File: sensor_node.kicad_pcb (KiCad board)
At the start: 2 copper layers, 92 parts, among them J1 Conn_01x06_Male, J2 Conn_01x03, J3 USB_B_Micro, J4 Conn_01x02_Female, J5 Conn_01x06_Male, J6 Conn_01x04_Male, J7 Conn_01x08_Male, Q1 Q_NMOS_DGS, Q2 Q_NMOS_DGS, Q3 Q_PMOS_DGS, Q4 Q_PMOS_DGS, SW1 SW_Push, SW2 SW_Push, U1 STM32L053R6Tx, U2 ESP-12F, U3 BME680, U4 Si1133, U5 USBLC6-2SC6, U6 BQ27441-G1, U7 BQ24075, U8 TPS826711, U9 LMZ21700, Y1 32.764kHz

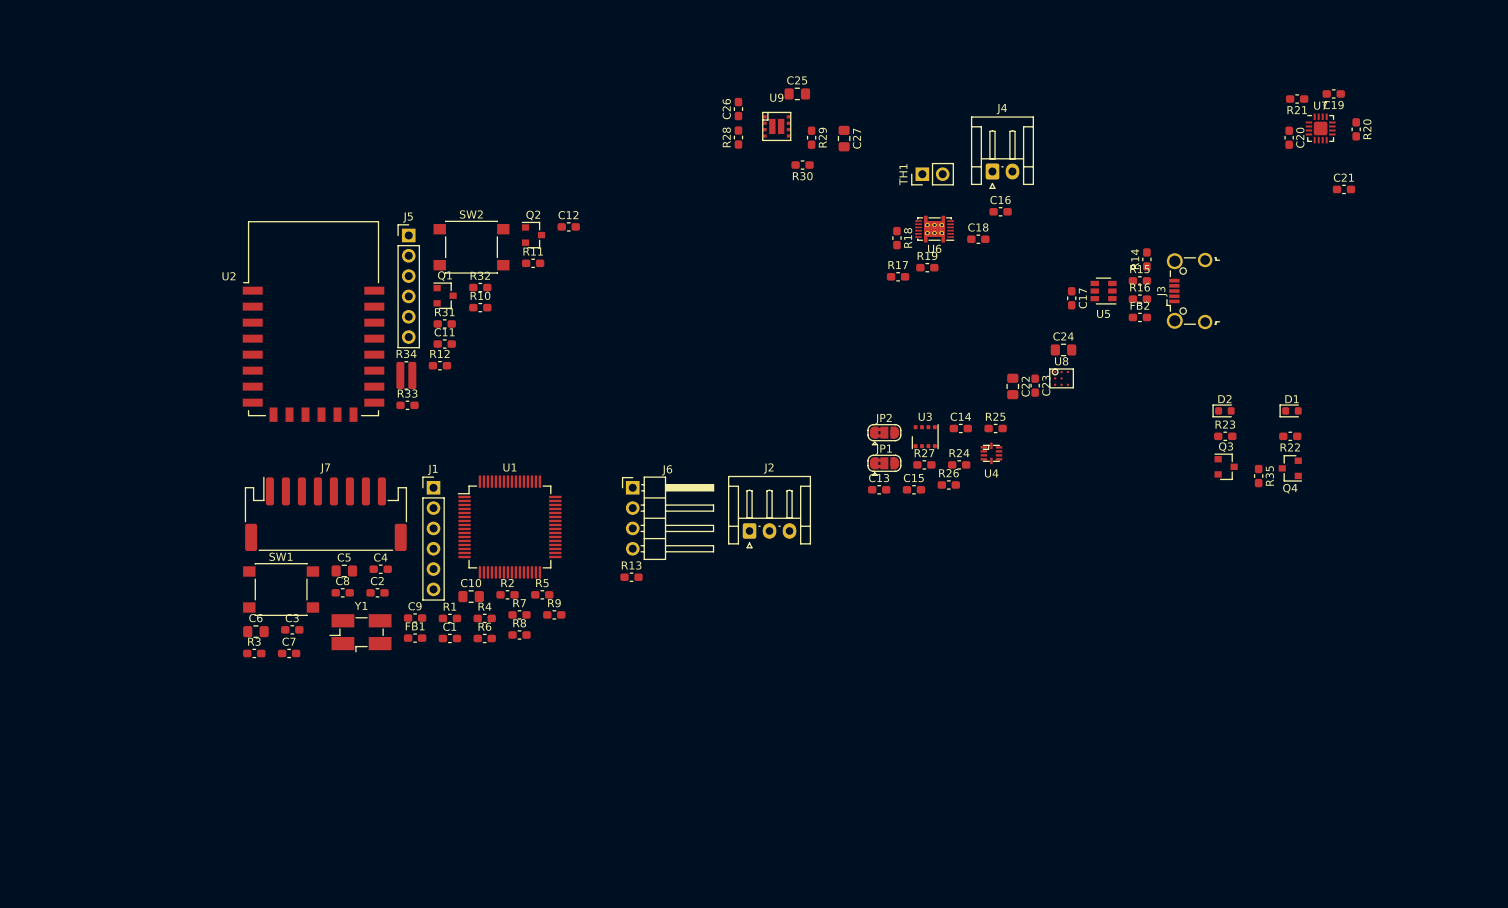
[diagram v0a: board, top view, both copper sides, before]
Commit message: work on layout and smaller changes to schematic
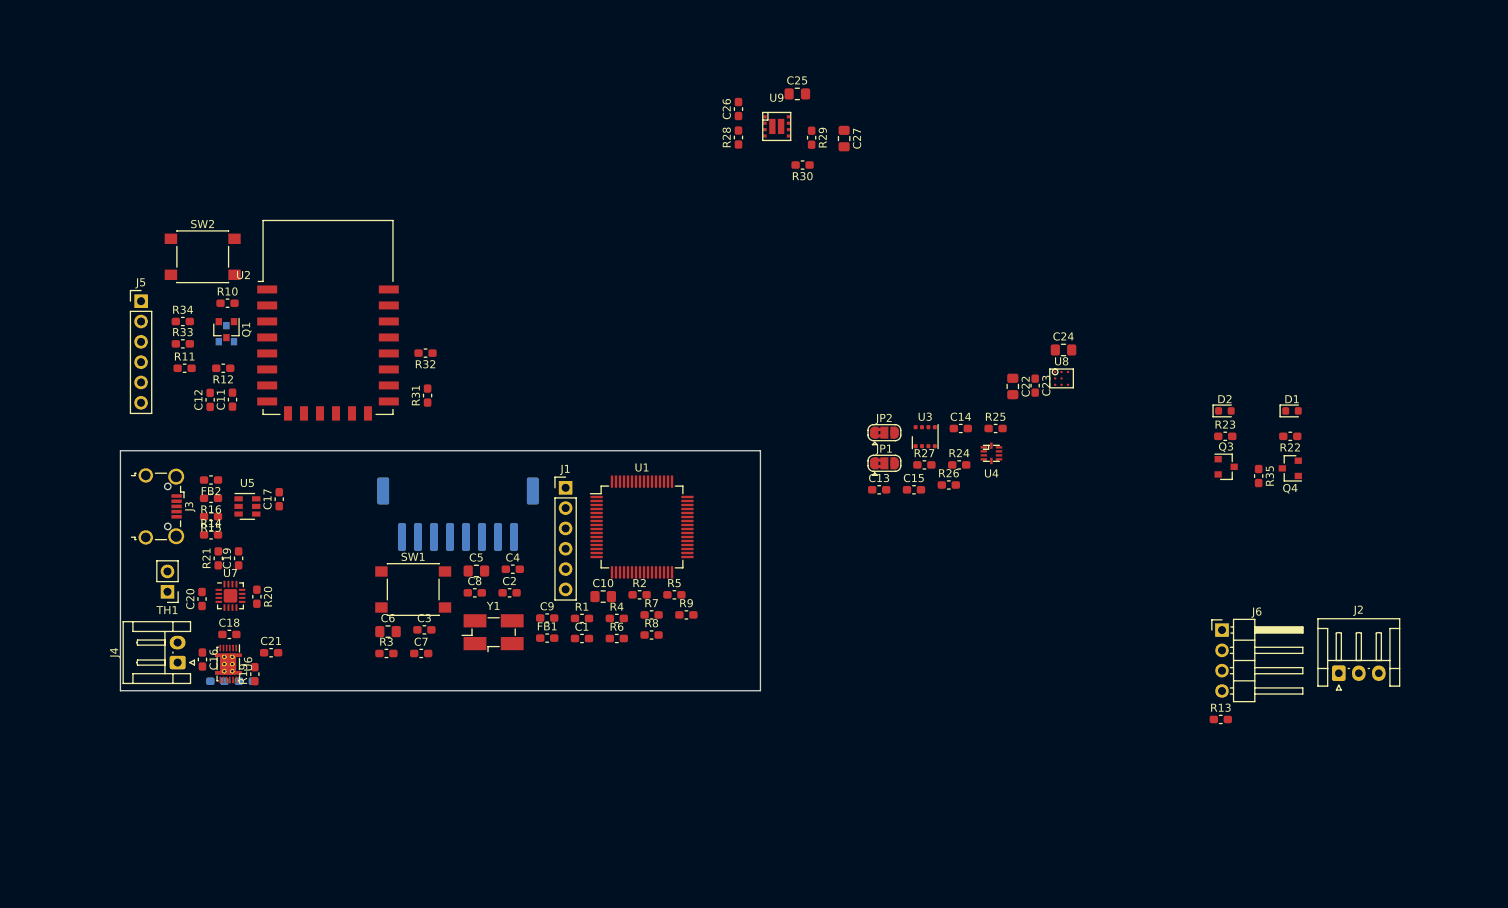
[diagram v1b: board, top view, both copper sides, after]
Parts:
- J7, Q2, R17, R18: moved to B.Cu
- R34: footprint Resistor_SMD:R_0612_1632Metric -> Resistor_SMD:R_0603_1608Metric_Pad1.05x0.95mm_HandSolder
- moved R20 149.3 mm to (67.1, 88.3)
- moved C19 148.7 mm to (64.8, 83.5), turned to 90 degrees
- moved U7 148.3 mm to (63.8, 88.1)
- moved C20 147.6 mm to (60.2, 88.5), turned to 90 degrees
- moved R21 146.6 mm to (62.2, 83.5), turned to 90 degrees
- moved C21 146.1 mm to (68.8, 95.2)
- moved J3 131.3 mm to (55.1, 77.0), turned to 270 degrees
- moved R14 121.9 mm to (61.3, 80.5), turned to 0 degrees
- moved R15 119.8 mm to (61.3, 78.2), turned to 180 degrees
- moved J4 118.9 mm to (57.1, 96.5), turned to 90 degrees
- moved R16 118.7 mm to (61.3, 75.9), turned to 180 degrees
- moved FB2 117.9 mm to (61.3, 73.7), turned to 180 degrees
- moved C16 114.4 mm to (60.2, 96.1), turned to 270 degrees
- moved U5 110.4 mm to (65.9, 77.0), turned to 0 degrees
- moved TH1 107.8 mm to (55.9, 87.6), turned to 180 degrees
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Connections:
- J4 pad 1: Net-(J4-Pad1) -> /power_supply/VBAT_P
- J4 pad 2: Net-(J4-Pad2) -> GND
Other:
- board outline added: 80 x 30 mm

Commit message: change mcu to smaller one
change connectors
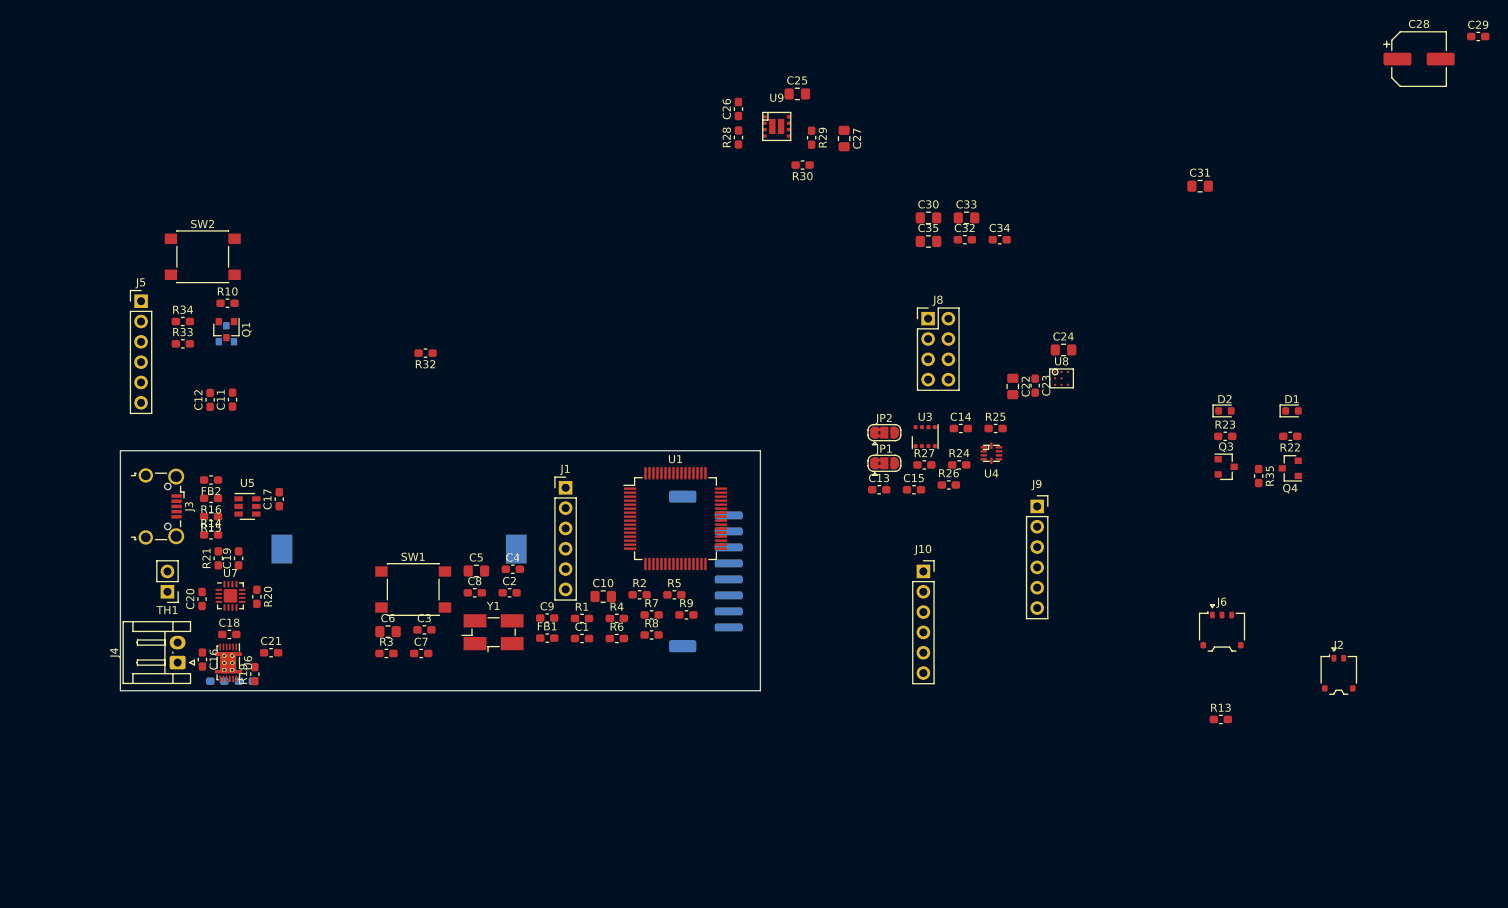
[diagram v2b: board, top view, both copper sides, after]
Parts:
- removed R11, R12, R31: 10k, Resistor_SMD:R_0603_1608Metric_Pad1.05x0.95mm_HandSolder
- removed U2: ESP-12F, RF_Module:ESP-12E
- added BT1: Battery_Cell, Battery:BatteryHolder_Keystone_1060_1x2032, B.Cu at (84.8, 82.3)
- added C28: 10uF, Capacitor_SMD:CP_Elec_6.3x3, F.Cu at (212.3, 21.0)
- added C29: 100nF, Capacitor_SMD:C_0603_1608Metric_Pad1.05x0.95mm_HandSolder, F.Cu at (219.7, 18.2)
- added C30: 10uF, Capacitor_SMD:C_0805_2012Metric_Pad1.15x1.40mm_HandSolder, F.Cu at (151.0, 40.9)
- added C31: 10uF, Capacitor_SMD:C_0805_2012Metric_Pad1.15x1.40mm_HandSolder, F.Cu at (185.0, 36.9)
- added C32: 100nF, Capacitor_SMD:C_0603_1608Metric_Pad1.05x0.95mm_HandSolder, F.Cu at (155.6, 43.6)
- added C33: 10uF, Capacitor_SMD:C_0805_2012Metric_Pad1.15x1.40mm_HandSolder, F.Cu at (155.8, 40.9)
- added C34: 100nF, Capacitor_SMD:C_0603_1608Metric_Pad1.05x0.95mm_HandSolder, F.Cu at (159.9, 43.6)
- added C35: 10uF, Capacitor_SMD:C_0805_2012Metric_Pad1.15x1.40mm_HandSolder, F.Cu at (151.0, 43.8)
- added J10: Conn_01x06, Connector_PinSocket_2.54mm:PinSocket_1x06_P2.54mm_Vertical, F.Cu at (150.4, 85.1)
- added J8: Conn_02x04_Odd_Even, Connector_PinHeader_2.54mm:PinHeader_2x04_P2.54mm_Vertical, F.Cu at (151.0, 53.5)
- added J9: Conn_01x06_Male, Connector_PinSocket_2.54mm:PinSocket_1x06_P2.54mm_Vertical, F.Cu at (164.6, 77.0)
- J2: footprint Connector_JST:JST_EH_S3B-EH_1x03_P2.50mm_Horizontal -> Connector_Molex:Molex_Pico-EZmate_78171-0002_1x02-1MP_P1.20mm_Vertical
- J6: footprint Connector_PinHeader_2.54mm:PinHeader_1x04_P2.54mm_Horizontal -> Connector_Molex:Molex_Pico-EZmate_78171-0003_1x03-1MP_P1.20mm_Vertical
- U1: value STM32L053R6Tx -> STM32L063R8Tx
- moved J7 31.8 mm to (123.2, 85.1), turned to 90 degrees
- moved U1 4.31 mm to (119.4, 78.5)
- moved U6 0.14 mm to (63.5, 96.5)
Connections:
- net /mcu.sch/PC0 renamed Net-(U1-Pad8)
- net /mcu.sch/PC1 renamed Net-(U1-Pad9)
- net /mcu.sch/PC10 renamed Net-(U1-Pad51)
- net /mcu.sch/PC11 renamed Net-(U1-Pad52)
- net /mcu.sch/PC12 renamed Net-(U1-Pad53)
- net /mcu.sch/PC13 renamed Net-(U1-Pad2)
- net /mcu.sch/PC14 renamed Net-(U1-Pad3)
- net /mcu.sch/PC15 renamed Net-(U1-Pad4)
- net /mcu.sch/PC2 renamed Net-(U1-Pad10)
- net /mcu.sch/PC3 renamed Net-(U1-Pad11)
- net /mcu.sch/PC4 renamed Net-(U1-Pad24)
- net /mcu.sch/PC5 renamed Net-(U1-Pad25)
- net /mcu.sch/PC6 renamed Net-(U1-Pad37)
- net /mcu.sch/PC7 renamed Net-(U1-Pad38)
- net /mcu.sch/PC8 renamed Net-(U1-Pad39)
- net /mcu.sch/PC9 renamed Net-(U1-Pad40)
- J5 pad 1: /ESP_RX -> /wireless/ESP_TX
- J5 pad 4: /ESP_TX -> /wireless/ESP_RX
- R5 pad 1: /mcu.sch/I2C1_SCL -> /SCL
- R6 pad 1: /mcu.sch/I2C1_SDA -> /SDA
- U1 pad 5: Net-(C8-Pad1) -> Net-(U1-Pad5)
- U1 pad 6: Net-(R1-Pad1) -> Net-(U1-Pad6)
- U1 pad 60: Net-(R2-Pad2) -> Net-(U1-Pad60)
- U1 pad 61: /mcu.sch/I2C1_SCL -> /SCL
- U1 pad 62: /mcu.sch/I2C1_SDA -> /SDA

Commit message: strip of some components and use more external modules
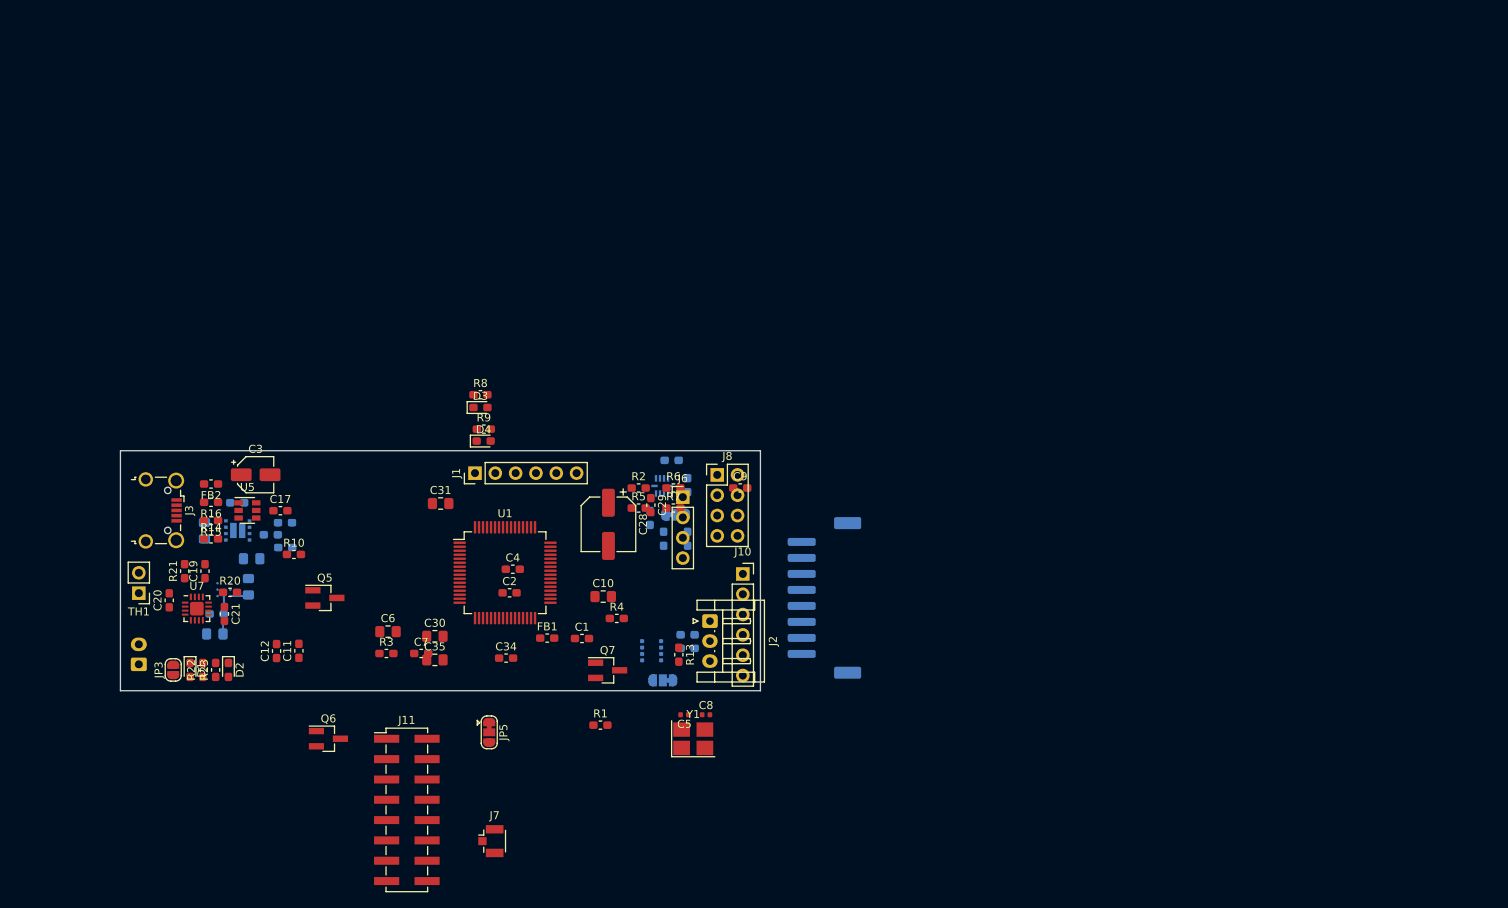
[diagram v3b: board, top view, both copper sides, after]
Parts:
- removed BT1: Battery_Cell, Battery:BatteryHolder_Keystone_1060_1x2032
- removed C16: 1uF, Capacitor_SMD:C_0603_1608Metric_Pad1.05x0.95mm_HandSolder
- removed C18: 0.47uF, Capacitor_SMD:C_0603_1608Metric_Pad1.05x0.95mm_HandSolder
- removed C32: 100nF, Capacitor_SMD:C_0603_1608Metric_Pad1.05x0.95mm_HandSolder
- removed C33: 10uF, Capacitor_SMD:C_0805_2012Metric_Pad1.15x1.40mm_HandSolder
- removed J9: Conn_01x06_Male, Connector_PinSocket_2.54mm:PinSocket_1x06_P2.54mm_Vertical
- removed Q1, Q2: Q_NMOS_DGS, Package_TO_SOT_SMD:SOT-23
- removed Q3, Q4: Q_PMOS_DGS, Package_TO_SOT_SMD:SOT-23
- removed R17: 10m, Resistor_SMD:R_0603_1608Metric_Pad1.05x0.95mm_HandSolder
- removed R18, R19, R32: 10k, Resistor_SMD:R_0603_1608Metric_Pad1.05x0.95mm_HandSolder
- removed R33, R34: R, Resistor_SMD:R_0603_1608Metric_Pad1.05x0.95mm_HandSolder
- removed R35: 20k, Resistor_SMD:R_0603_1608Metric_Pad1.05x0.95mm_HandSolder
- removed SW1, SW2: SW_Push, Button_Switch_SMD:SW_Push_1P1T_NO_6x6mm_H9.5mm
- removed U6: BQ27441-G1, Package_SON:Texas_S-PDSO-N12
- added D3: LED, LED_SMD:LED_0603_1608Metric_Pad1.05x0.95mm_HandSolder, F.Cu at (95.0, 64.6)
- added D4: LED, LED_SMD:LED_0603_1608Metric_Pad1.05x0.95mm_HandSolder, F.Cu at (95.4, 68.8)
- added J11: Conn_02x08_Counter_Clockwise, Connector_PinHeader_2.54mm:PinHeader_2x08_P2.54mm_Vertical_SMD, F.Cu at (85.8, 114.9)
- added JP3: Jumper_2_Open, Jumper:SolderJumper-2_P1.3mm_Open_RoundedPad1.0x1.5mm, F.Cu at (56.6, 97.4)
- added JP5: SolderJumper_3_Bridged12, Jumper:SolderJumper-3_P1.3mm_Bridged12_RoundedPad1.0x1.5mm, F.Cu at (96.1, 105.2)
- added Q5: Q_PMOS_GSD, Package_TO_SOT_SMD:SOT-23_Handsoldering, F.Cu at (75.5, 88.4)
- added Q6: Q_PMOS_GSD, Package_TO_SOT_SMD:SOT-23_Handsoldering, F.Cu at (76.0, 106.0)
- added Q7: Q_PMOS_GSD, Package_TO_SOT_SMD:SOT-23_Handsoldering, F.Cu at (110.9, 97.4)
- C13, C14, C15, C22, C23, C24, C25, C26, C27, J4, R24, R25, R26, R27, R28, R29, R30, U3, U4, U8, U9: moved to B.Cu
- C3: value 100nF -> 10uF; footprint Capacitor_SMD:C_0603_1608Metric_Pad1.05x0.95mm_HandSolder -> Capacitor_SMD:CP_Elec_4x5.7
- C5: value 10uF -> 10pF; footprint Capacitor_SMD:C_0805_2012Metric_Pad1.15x1.40mm_HandSolder -> Capacitor_SMD:C_0402_1005Metric
- C8: value C -> 10pF; footprint Capacitor_SMD:C_0603_1608Metric_Pad1.05x0.95mm_HandSolder -> Capacitor_SMD:C_0402_1005Metric
- C9: value C -> 100nF; footprint Capacitor_SMD:C_0603_1608Metric_Pad1.05x0.95mm_HandSolder -> Resistor_SMD:R_0603_1608Metric_Pad1.05x0.95mm_HandSolder
- D1, D2: footprint LED_SMD:LED_0603_1608Metric -> LED_SMD:LED_0603_1608Metric_Pad1.05x0.95mm_HandSolder
- J2: footprint Connector_Molex:Molex_Pico-EZmate_78171-0002_1x02-1MP_P1.20mm_Vertical -> Connector_JST:JST_EH_S3B-EH_1x03_P2.50mm_Horizontal
- J5: value Conn_01x06_Male -> Conn_01x08_Male; footprint Connector_PinHeader_2.54mm:PinHeader_1x06_P2.54mm_Vertical -> Connector_JST:JST_PH_S8B-PH-SM4-TB_1x08-1MP_P2.00mm_Horizontal; moved to B.Cu
- J6: footprint Connector_Molex:Molex_Pico-EZmate_78171-0003_1x03-1MP_P1.20mm_Vertical -> Connector_PinHeader_2.54mm:PinHeader_1x04_P2.54mm_Vertical
- J7: value Conn_01x08_Male -> Conn_Coaxial; footprint Connector_JST:JST_PH_S8B-PH-SM4-TB_1x08-1MP_P2.00mm_Horizontal -> Connector_Coaxial:U.FL_Hirose_U.FL-R-SMT-1_Vertical; moved to F.Cu
- JP1, JP2: footprint Jumper:SolderJumper-3_P1.3mm_Bridged2Bar12_RoundedPad1.0x1.5mm -> Jumper:SolderJumper-3_P1.3mm_Bridged12_RoundedPad1.0x1.5mm; moved to B.Cu
- R1: value R -> 10k
- R2: value R -> 4k7
- R8: value 4k7 -> R
- R9: value 10k -> R
- Y1: value 32.764kHz -> Crystal_GND24; footprint Crystal:Crystal_SMD_EuroQuartz_MJ-4Pin_5.0x3.2mm_HandSoldering -> Crystal:Crystal_SMD_TXC_7M-4Pin_3.2x2.5mm_HandSoldering
- moved D1 141.5 mm to (58.7, 97.4), turned to 270 degrees
- moved R22 139.0 mm to (60.3, 97.4), turned to 90 degrees
- moved R23 129.5 mm to (61.9, 97.4), turned to 90 degrees
- moved D2 128.7 mm to (63.5, 97.4), turned to 270 degrees
- moved C29 118.9 mm to (116.3, 76.8), turned to 270 degrees
- moved C28 116.8 mm to (111.0, 79.2), turned to 270 degrees
- moved U8 108.0 mm to (62.9, 87.4), turned to 90 degrees
- moved C23 106.2 mm to (62.0, 90.4), turned to 180 degrees
- moved C24 106.1 mm to (66.0, 87.0), turned to 90 degrees
- moved C22 104.4 mm to (61.8, 92.9), turned to 180 degrees
- moved C31 102.9 mm to (90.0, 76.6)
- moved J5 93.1 mm to (138.0, 88.4), turned to 270 degrees
- moved C25 92.1 mm to (60.5, 80.0), turned to 270 degrees
- moved C27 90.8 mm to (66.4, 83.5), turned to 180 degrees
- moved U9 84.2 mm to (64.7, 80.0), turned to 180 degrees
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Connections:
- net /EXT_GPIO0 renamed /PC3
- net /PC9 renamed /PC13
- net /mcu.sch/DSIP_BUSY renamed /mcu.sch/PA10
- net /mcu.sch/SPI1_MISO renamed /mcu.sch/PA6
- net /mcu.sch/SWCLK renamed /mcu.sch/PA14
- net /mcu.sch/SWDIO renamed /mcu.sch/PA13
- net /mcu.sch/USART1_RX renamed /STM_PB7
- net /mcu.sch/USART1_TX renamed /STM_PB6
- net /mcu.sch/USB_DN renamed /mcu.sch/PA11
- net /mcu.sch/USB_DP renamed /mcu.sch/PA12
- net Net-(U1-Pad10) renamed /mcu.sch/PC2
- net Net-(U1-Pad11) renamed /mcu.sch/PC3
- net Net-(U1-Pad2) renamed /mcu.sch/PC13
- net Net-(U1-Pad24) renamed /mcu.sch/PC4
- net Net-(U1-Pad25) renamed /mcu.sch/PC5
- net Net-(U1-Pad3) renamed /mcu.sch/PC14
- net Net-(U1-Pad37) renamed /mcu.sch/PC6
- net Net-(U1-Pad38) renamed /mcu.sch/PC7
- net Net-(U1-Pad39) renamed /mcu.sch/PC8
- net Net-(U1-Pad4) renamed /mcu.sch/PC15
- net Net-(U1-Pad40) renamed /mcu.sch/PC9
- net Net-(U1-Pad51) renamed /mcu.sch/PC10
- net Net-(U1-Pad52) renamed /mcu.sch/PC11
- net Net-(U1-Pad53) renamed /mcu.sch/PC12
- net Net-(U1-Pad8) renamed /mcu.sch/PC0
- net Net-(U1-Pad9) renamed /mcu.sch/PC1
- C11 pad 1: /VCC_1V8 -> /wireless/VCC_ESP
- C12 pad 1: /VCC_1V8 -> /wireless/VCC_ESP
- C13 pad 1: /VCC_3V3 -> /sensors/VCC_SENSORS
- C14 pad 1: /VCC_3V3 -> /sensors/VCC_SENSORS
- C15 pad 1: /VCC_3V3 -> /sensors/VCC_SENSORS
- C3 pad 1: /mcu.sch/VREF -> /power_supply/VUSB
- C34 pad 1: /VCC_1V8 -> /mcu.sch/STM_VUSB
- C35 pad 1: /VCC_1V8 -> /mcu.sch/STM_VUSB
- C5 pad 1: /mcu.sch/VREF -> /mcu.sch/OSC_0
- C5 pad 2: GND -> Net-(C5-Pad2)
- C8 pad 1: Net-(C8-Pad1) -> /mcu.sch/OSC_1
- C8 pad 2: GND -> Net-(C5-Pad2)
- C9 pad 1: Net-(C9-Pad1) -> /mcu.sch/NRST
- D1 pad 1: /PB0 -> /PC5
- D2 pad 1: /PB0 -> /PC4
- J10 pad 3: /EXT_GPIO1 -> /PC4
- J10 pad 4: /EXT_GPIO2 -> /PC4
- J10 pad 5: /EXT_GPIO3 -> /PC5
- J3 pad 6: GND -> Net-(J3-Pad6)
- J4 pad 1: /power_supply/VBAT_P -> /power_supply/VBAT
- J5 pad 1: /wireless/ESP_TX -> /VCC_3V3
- J5 pad 2: /wireless/ESP_DTR -> GND
- J5 pad 3: /wireless/ESP_RTS -> /SPI1_MOSI
- J5 pad 4: /wireless/ESP_RX -> /SPI1_SCK
- J5 pad 5: Net-(J5-Pad5) -> /SPI1_NSS
- J5 pad 6: GND -> /DISP_DC
- J6 pad 2: /SDA -> /I2C1_SDA
- J7 pad 1: /mcu.sch/VCC_3V3 -> /sensors/GPS_TIMEPULSE
- J8 pad 1: /wireless/ESP_RX -> /ESP_TX
- J8 pad 2: /VCC_1V8 -> /wireless/VCC_ESP
- J8 pad 8: /wireless/ESP_TX -> /ESP_RX
- JP1 pad 1: /VCC_3V3 -> /sensors/VCC_SENSORS
- R1 pad 2: Net-(C9-Pad1) -> GND
- R10 pad 1: /VCC_1V8 -> /wireless/VCC_ESP
- R2 pad 1: /VCC_1V8 -> /I2C1_SCL
- R2 pad 2: Net-(R2-Pad2) -> /VCC_3V3
- R22 pad 1: Net-(Q4-Pad1) -> Net-(JP3-Pad1)
- R23 pad 1: VIN -> Net-(JP3-Pad1)
- R24 pad 2: /VCC_3V3 -> /sensors/VCC_SENSORS
- R25 pad 1: /VCC_3V3 -> /sensors/VCC_SENSORS
- R26 pad 1: /VCC_3V3 -> /sensors/VCC_SENSORS
- R3 pad 2: Net-(R3-Pad2) -> /mcu.sch/STM_VUSB
- R4 pad 1: Net-(R3-Pad2) -> /mcu.sch/STM_VUSB
- R5 pad 1: /SCL -> /I2C1_SDA
- R5 pad 2: /mcu.sch/VCC_3V3 -> /VCC_3V3
- R6 pad 1: /SDA -> /I2C2_SCL
- R6 pad 2: /mcu.sch/VCC_3V3 -> /VCC_3V3
- R7 pad 1: /SCL -> /I2C2_SDA
- R7 pad 2: /mcu.sch/VCC_3V3 -> /VCC_3V3
- R8 pad 1: /SDA -> Net-(D3-Pad1)
- R8 pad 2: /mcu.sch/VCC_3V3 -> GND
- R9 pad 1: /VCC_1V8 -> Net-(D4-Pad1)
- R9 pad 2: /mcu.sch/NRST -> GND
- U1 pad 16: /ESP_RX -> /EXP_RX
- U1 pad 17: /EXP_TX -> /ESP_TX
- U1 pad 20: /mcu.sch/SPI1_NSS -> /SPI1_NSS
- U1 pad 21: /mcu.sch/SPI1_SCK -> /mcu.sch/PA5
- U1 pad 23: /mcu.sch/SPI1_MOSI -> /mcu.sch/PA7
- U1 pad 29: /SCL -> /mcu.sch/PB10
- U1 pad 30: /SDA -> /mcu.sch/PB11
- U1 pad 41: /mcu.sch/DISP_DC -> /mcu.sch/PA8
- U1 pad 42: /mcu.sch/DISP_RST -> /mcu.sch/PA9
- U1 pad 48: Net-(R3-Pad2) -> /mcu.sch/STM_VUSB
- U1 pad 5: Net-(U1-Pad5) -> /mcu.sch/OSC_0
- U1 pad 6: Net-(U1-Pad6) -> /mcu.sch/OSC_1
- U1 pad 60: Net-(U1-Pad60) -> Net-(R1-Pad1)
- U1 pad 61: /SCL -> /I2C1_SCL
- U1 pad 62: /SDA -> /I2C1_SDA
- U3 pad 2: /VCC_3V3 -> /sensors/VCC_SENSORS
- U3 pad 3: /SDA -> /I2C2_SDA
- U3 pad 4: /SCL -> /I2C2_SCL
- U3 pad 6: /VCC_3V3 -> /sensors/VCC_SENSORS
- U3 pad 8: /VCC_3V3 -> /sensors/VCC_SENSORS
- U4 pad 1: /SDA -> /I2C2_SDA
- U4 pad 2: /SCL -> /I2C2_SCL
- U4 pad 3: /VCC_3V3 -> /sensors/VCC_SENSORS
- U7 pad 17: Net-(U7-Pad17) -> GND
- U7 pad 7: /PB0 -> /PC5
- U7 pad 9: /PB0 -> /PC4
- Y1 pad 1: Net-(C8-Pad1) -> /mcu.sch/OSC_0
- Y1 pad 2: Net-(C9-Pad1) -> Net-(Y1-Pad2)
- Y1 pad 3: (no net) -> /mcu.sch/OSC_1
- Y1 pad 4: (no net) -> Net-(Y1-Pad4)
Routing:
- net VIN: track 0.00 -> 4.93 mm
- net /VCC_1V8: track 0.00 -> 2.37 mm
